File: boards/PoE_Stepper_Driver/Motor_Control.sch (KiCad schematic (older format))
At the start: 3 parts

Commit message: pretty much finished motor subsystem schematic
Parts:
- removed U?: TMC2660C-PA, QFP_2660C-PA_TRI, symbol TMC2660C-PA:TMC2660C-PA
- added C? (x2): 0.1uF, symbol device:C_Small
- added C? (x2): 10nF, symbol device:C_Small
- added C?: 470nF, symbol device:C_Small
- added C?: 220nF, symbol device:C_Small
- added C? (x2): 10uF, symbol device:C_Small
- added C? (x2): 100uF, symbol device:CP1_Small
- added R? (x3): 10k, symbol device:R_Small
- added R? (x2): 22, symbol device:R_Small
- added R? (x2): 75m, symbol device:R_Small
- added SW?: STO_L, symbol Switch:SW_SPST
- added SW?: STO_R, symbol Switch:SW_SPST
- added U?: TMC2660C-PA, QFP_2660C-PA_TRI, symbol TMC2660_2:TMC2660C-PA
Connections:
- net labels added: +12V, +3V3, CLK_2660, CLK_429, DIR, SPI1_CS, SPI1_MISO, SPI1_MOSI, SPI2_CS, SPI2_MISO, SPI2_MOSI, SPI2_SCK, STEP
- net labels removed: OA1, OA2, OB1, OB2
- wire segments 32 -> 150
- no-connect marks 0 -> 4
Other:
- moved on the sheet: J?, U?

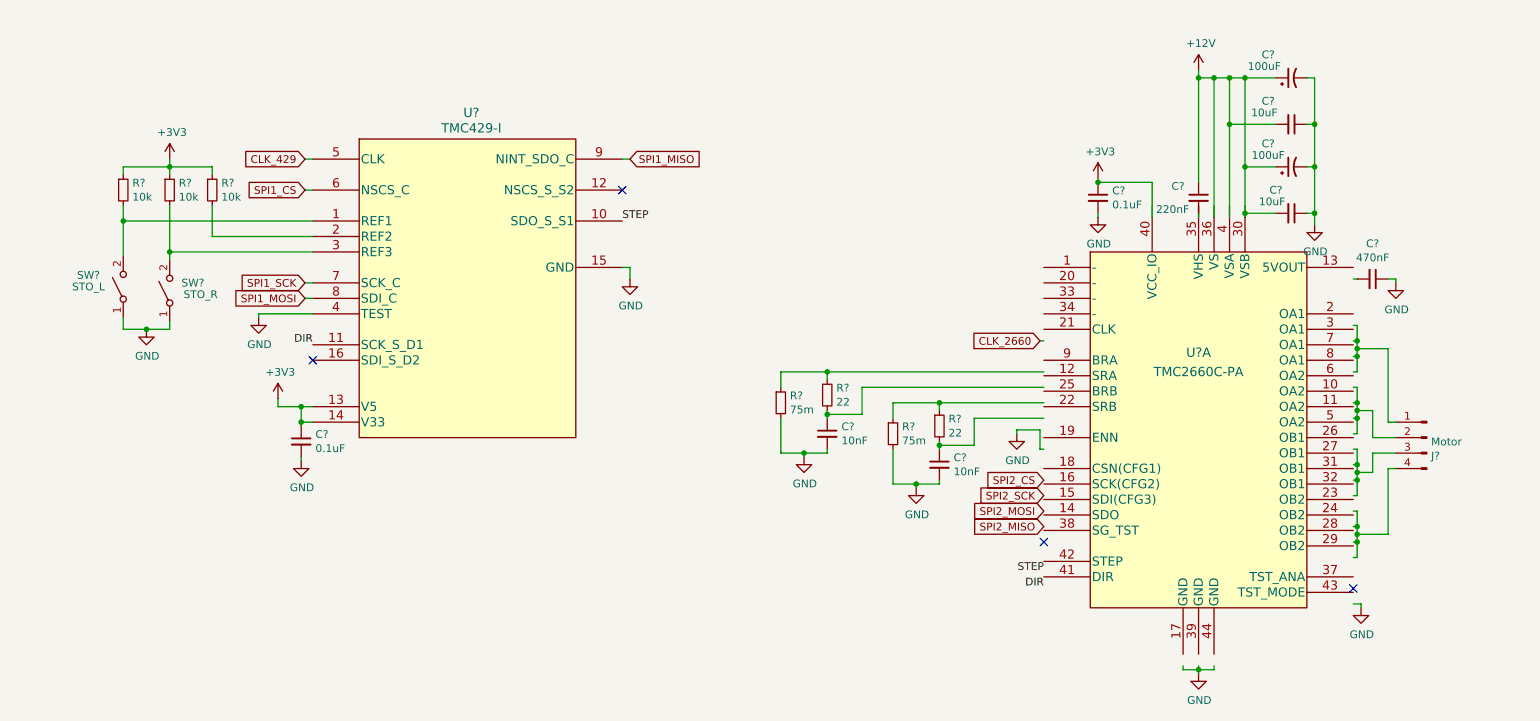
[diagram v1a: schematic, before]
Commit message: added actual phy
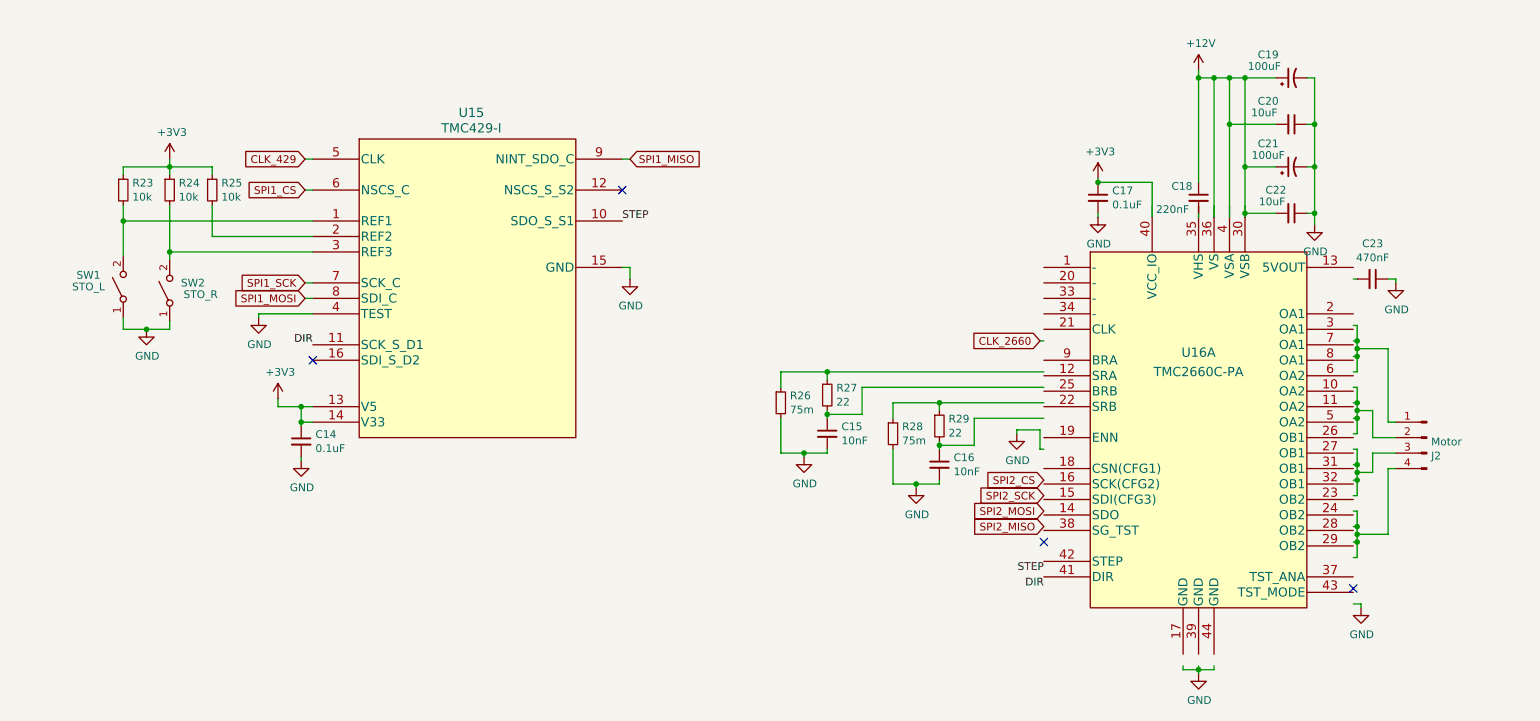
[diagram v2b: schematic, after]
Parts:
- gave numbers to parts that had none: 22
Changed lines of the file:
@@
 encoding utf-8
 Sheet 3 3
-Title ""
-Date ""
-Rev ""
+Title "PoE Stepper Driver"
+Date "2022-02-22"
+Rev "1.0"
 Comp ""
 Comment1 ""
@@
 $EndDescr
 $Comp
-L TMC429-I:TMC429-I U?
+L TMC429-I:TMC429-I U15
 U 1 1 6293383B
 P 2775 2300
-F 0 "U?" H 3800 2600 60  0000 C CNN
+F 0 "U15" H 3800 2600 60  0000 C CNN
 F 1 "TMC429-I" H 3800 2500 60  0000 C CNN
 F 2 "SSOP16_150MIL_TRI" H 3975 2540 60  0001 C CNN
@@
 SPI1_SCK
 $Comp
-L power:GND #PWR?
+L power:GND #PWR027
 U 1 1 62939459
 P 4825 3075
-F 0 "#PWR?" H 4825 2825 50  0001 C CNN
+F 0 "#PWR027" H 4825 2825 50  0001 C CNN
 F 1 "GND" H 4830 2902 50  0000 C CNN
 F 2 "" H 4825 3075 50  0001 C CNN
@@
 	4825 3000 4825 3075
 $Comp
-L power:GND #PWR?
+L power:GND #PWR034
 U 1 1 6293B082
 P 8500 5625
-F 0 "#PWR?" H 8500 5375 50  0001 C CNN
+F 0 "#PWR034" H 8500 5375 50  0001 C CNN
 F 1 "GND" H 8505 5452 50  0000 C CNN
 F 2 "" H 8500 5625 50  0001 C CNN
@@
 P 7850 2550
 AR Path="/6218906C" Ref="C?"  Part="1"
-AR Path="/6293177D/6218906C" Ref="C?"  Part="1"
-F 0 "C?" H 7942 2596 50  0000 L CNN
+AR Path="/6293177D/6218906C" Ref="C17"  Part="1"
+F 0 "C17" H 7942 2596 50  0000 L CNN
 F 1 "0.1uF" H 7942 2505 50  0000 L CNN
 F 2 "" H 7850 2550 50  0001 C CNN
@@
 P 7850 2425
 AR Path="/62189079" Ref="#PWR?"  Part="1"
-AR Path="/6293177D/62189079" Ref="#PWR?"  Part="1"
-F 0 "#PWR?" H 7850 2275 50  0001 C CNN
+AR Path="/6293177D/62189079" Ref="#PWR031"  Part="1"
+F 0 "#PWR031" H 7850 2275 50  0001 C CNN
 F 1 "+3V3" H 7865 2598 50  0000 C CNN
 F 2 "" H 7850 2425 50  0001 C CNN
@@
 P 2550 3850
 AR Path="/6218AB1A" Ref="#PWR?"  Part="1"
-AR Path="/6293177D/6218AB1A" Ref="#PWR?"  Part="1"
-F 0 "#PWR?" H 2550 3700 50  0001 C CNN
+AR Path="/6293177D/6218AB1A" Ref="#PWR025"  Part="1"
+F 0 "#PWR025" H 2550 3700 50  0001 C CNN
 F 1 "+3V3" H 2565 4023 50  0000 C CNN
 F 2 "" H 2550 3850 50  0001 C CNN
@@
 $EndComp
 $Comp
-L Switch:SW_SPST SW?
+L Switch:SW_SPST SW1
 U 1 1 6218BE4E
 P 1550 3125
-F 0 "SW?" V 1625 3350 50  0000 C CNN
+F 0 "SW1" V 1625 3350 50  0000 C CNN
 F 1 "STO_L" V 1550 3350 50  0000 C CNN
 F 2 "" H 1550 3125 50  0001 C CNN
@@
 $EndComp
 $Comp
-L Switch:SW_SPST SW?
+L Switch:SW_SPST SW2
 U 1 1 6218DF68
 P 1850 3150
-F 0 "SW?" V 1900 3000 50  0000 C CNN
+F 0 "SW2" V 1900 3000 50  0000 C CNN
 F 1 "STO_R" V 1825 2950 50  0000 C CNN
 F 2 "" H 1850 3150 50  0001 C CNN
@@
 $EndComp
 $Comp
-L power:GND #PWR?
+L power:GND #PWR024
 U 1 1 62192B2C
 P 2425 3325
-F 0 "#PWR?" H 2425 3075 50  0001 C CNN
+F 0 "#PWR024" H 2425 3075 50  0001 C CNN
 F 1 "GND" H 2430 3152 50  0000 C CNN
 F 2 "" H 2425 3325 50  0001 C CNN
@@
 NoConn ~ 4775 2500
 $Comp
-L device:C_Small C?
+L device:C_Small C14
 U 1 1 6219FF35
 P 2700 4125
-F 0 "C?" H 2608 4171 50  0000 R CNN
+F 0 "C14" H 2608 4171 50  0000 R CNN
 F 1 "0.1uF" H 2608 4080 50  0000 R CNN
 F 2 "" H 2700 4125 50  0001 C CNN
@@
 	2700 4000 2700 4025
 $Comp
-L power:GND #PWR?
+L power:GND #PWR026
 U 1 1 621A3739
 P 2700 4250
-F 0 "#PWR?" H 2700 4000 50  0001 C CNN
+F 0 "#PWR026" H 2700 4000 50  0001 C CNN
 F 1 "GND" H 2705 4077 50  0000 C CNN
 F 2 "" H 2700 4250 50  0001 C CNN
@@
 	2725 2300 2775 2300
 $Comp
-L power:GND #PWR?
+L power:GND #PWR022
 U 1 1 621E2D05
 P 1700 3400
-F 0 "#PWR?" H 1700 3150 50  0001 C CNN
+F 0 "#PWR022" H 1700 3150 50  0001 C CNN
 F 1 "GND" H 1705 3227 50  0000 C CNN
 F 2 "" H 1700 3400 50  0001 C CNN
@@
 	1550 2700 2775 2700
 $Comp
-L device:R_Small R?
+L device:R_Small R23
 U 1 1 621F05A6
 P 1550 2500
-F 0 "R?" H 1609 2546 50  0000 L CNN
+F 0 "R23" H 1609 2546 50  0000 L CNN
 F 1 "10k" H 1609 2455 50  0000 L CNN
 F 2 "" H 1550 2500 50  0001 C CNN
@@
 $EndComp
 $Comp
-L device:R_Small R?
+L device:R_Small R24
 U 1 1 621F9F83
 P 1850 2500
-F 0 "R?" H 1909 2546 50  0000 L CNN
+F 0 "R24" H 1909 2546 50  0000 L CNN
 F 1 "10k" H 1909 2455 50  0000 L CNN
 F 2 "" H 1850 2500 50  0001 C CNN
@@
 $EndComp
 $Comp
-L device:R_Small R?
+L device:R_Small R25
 U 1 1 62202E57
 P 2125 2500
-F 0 "R?" H 2184 2546 50  0000 L CNN
+F 0 "R25" H 2184 2546 50  0000 L CNN
 F 1 "10k" H 2184 2455 50  0000 L CNN
 F 2 "" H 2125 2500 50  0001 C CNN
@@
 P 1850 2300
 AR Path="/62208E6C" Ref="#PWR?"  Part="1"
-AR Path="/6293177D/62208E6C" Ref="#PWR?"  Part="1"
-F 0 "#PWR?" H 1850 2150 50  0001 C CNN
+AR Path="/6293177D/62208E6C" Ref="#PWR023"  Part="1"
+F 0 "#PWR023" H 1850 2150 50  0001 C CNN
 F 1 "+3V3" H 1865 2473 50  0000 C CNN
 F 2 "" H 1850 2300 50  0001 C CNN
@@
 P 9975 4100
 AR Path="/6292FF7A/62931FC4" Ref="J?"  Part="1"
-AR Path="/6293177D/62931FC4" Ref="J?"  Part="1"
-F 0 "J?" H 9947 3982 50  0000 R CNN
+AR Path="/6293177D/62931FC4" Ref="J2"  Part="1"
+F 0 "J2" H 9947 3982 50  0000 R CNN
 F 1 "Motor" H 9947 4073 50  0000 R CNN
 F 2 "" H 9975 4100 50  0001 C CNN
@@
 DIR
 $Comp
-L power:+12V #PWR?
+L power:+12V #PWR033
 U 1 1 622729F2
 P 8500 1725
-F 0 "#PWR?" H 8500 1575 50  0001 C CNN
+F 0 "#PWR033" H 8500 1575 50  0001 C CNN
 F 1 "+12V" H 8515 1898 50  0000 C CNN
 F 2 "" H 8500 1725 50  0001 C CNN
@@
 $EndComp
 $Comp
-L power:GND #PWR?
+L power:GND #PWR032
 U 1 1 6227F9C4
 P 7850 2675
-F 0 "#PWR?" H 7850 2425 50  0001 C CNN
+F 0 "#PWR032" H 7850 2425 50  0001 C CNN
 F 1 "GND" H 7855 2502 50  0000 C CNN
 F 2 "" H 7850 2675 50  0001 C CNN
@@
 	7850 2650 7850 2675
 $Comp
-L power:GND #PWR?
+L power:GND #PWR035
 U 1 1 62283BD0
 P 9250 2725
-F 0 "#PWR?" H 9250 2475 50  0001 C CNN
+F 0 "#PWR035" H 9250 2475 50  0001 C CNN
 F 1 "GND" H 9255 2552 50  0000 C CNN
 F 2 "" H 9250 2725 50  0001 C CNN
@@
 $EndComp
 $Comp
-L power:GND #PWR?
+L power:GND #PWR036
 U 1 1 622AA972
 P 9550 5200
-F 0 "#PWR?" H 9550 4950 50  0001 C CNN
+F 0 "#PWR036" H 9550 4950 50  0001 C CNN
 F 1 "GND" H 9555 5027 50  0000 C CNN
 F 2 "" H 9550 5200 50  0001 C CNN
@@
 SPI2_CS
 $Comp
-L device:R_Small R?
+L device:R_Small R27
 U 1 1 6238B615
 P 6100 3825
-F 0 "R?" H 6159 3871 50  0000 L CNN
+F 0 "R27" H 6159 3871 50  0000 L CNN
 F 1 "22" H 6159 3780 50  0000 L CNN
 F 2 "" H 6100 3825 50  0001 C CNN
@@
 $EndComp
 $Comp
-L device:C_Small C?
+L device:C_Small C15
 U 1 1 6238BD65
 P 6100 4075
-F 0 "C?" H 6192 4121 50  0000 L CNN
+F 0 "C15" H 6192 4121 50  0000 L CNN
 F 1 "10nF" H 6192 4030 50  0000 L CNN
 F 2 "" H 6100 4075 50  0001 C CNN
@@
 $EndComp
 $Comp
-L device:R_Small R?
+L device:R_Small R26
 U 1 1 623914C8
 P 5800 3875
-F 0 "R?" H 5859 3921 50  0000 L CNN
+F 0 "R26" H 5859 3921 50  0000 L CNN
 F 1 "75m" H 5859 3830 50  0000 L CNN
 F 2 "" H 5800 3875 50  0001 C CNN
@@
 $EndComp
 $Comp
-L power:GND #PWR?
+L power:GND #PWR028
 U 1 1 62397C91
 P 5950 4225
-F 0 "#PWR?" H 5950 3975 50  0001 C CNN
+F 0 "#PWR028" H 5950 3975 50  0001 C CNN
 F 1 "GND" H 5955 4052 50  0000 C CNN
 F 2 "" H 5950 4225 50  0001 C CNN
@@
 	6100 3950 6100 3975
 $Comp
-L device:R_Small R?
+L device:R_Small R29
 U 1 1 623F4B4C
 P 6825 4025
-F 0 "R?" H 6884 4071 50  0000 L CNN
+F 0 "R29" H 6884 4071 50  0000 L CNN
 F 1 "22" H 6884 3980 50  0000 L CNN
 F 2 "" H 6825 4025 50  0001 C CNN
@@
 $EndComp
 $Comp
-L device:C_Small C?
+L device:C_Small C16
 U 1 1 623F4B52
 P 6825 4275
-F 0 "C?" H 6917 4321 50  0000 L CNN
+F 0 "C16" H 6917 4321 50  0000 L CNN
 F 1 "10nF" H 6917 4230 50  0000 L CNN
 F 2 "" H 6825 4275 50  0001 C CNN
@@
 $EndComp
 $Comp
-L device:R_Small R?
+L device:R_Small R28
 U 1 1 623F4B58
 P 6525 4075
-F 0 "R?" H 6584 4121 50  0000 L CNN
+F 0 "R28" H 6584 4121 50  0000 L CNN
 F 1 "75m" H 6584 4030 50  0000 L CNN
 F 2 "" H 6525 4075 50  0001 C CNN
@@
 $EndComp
 $Comp
-L power:GND #PWR?
+L power:GND #PWR029
 U 1 1 623F4B5E
 P 6675 4425
-F 0 "#PWR?" H 6675 4175 50  0001 C CNN
+F 0 "#PWR029" H 6675 4175 50  0001 C CNN
 F 1 "GND" H 6680 4252 50  0000 C CNN
 F 2 "" H 6675 4425 50  0001 C CNN
@@
 NoConn ~ 9500 5075
 $Comp
-L power:GND #PWR?
+L power:GND #PWR037
 U 1 1 6246A24C
 P 9775 3100
-F 0 "#PWR?" H 9775 2850 50  0001 C CNN
+F 0 "#PWR037" H 9775 2850 50  0001 C CNN
 F 1 "GND" H 9780 2927 50  0000 C CNN
 F 2 "" H 9775 3100 50  0001 C CNN
@@
 	9500 3075 9525 3075
 $Comp
-L device:C_Small C?
+L device:C_Small C23
 U 1 1 62483CF6
 P 9625 3075
-F 0 "C?" V 9396 3075 50  0000 C CNN
+F 0 "C23" V 9396 3075 50  0000 C CNN
 F 1 "470nF" V 9487 3075 50  0000 C CNN
 F 2 "" H 9625 3075 50  0001 C CNN
@@
 	9775 3075 9775 3100
 $Comp
-L power:GND #PWR?
+L power:GND #PWR030
 U 1 1 624936CE
 P 7325 4075
-F 0 "#PWR?" H 7325 3825 50  0001 C CNN
+F 0 "#PWR030" H 7325 3825 50  0001 C CNN
 F 1 "GND" H 7330 3902 50  0000 C CNN
 F 2 "" H 7325 4075 50  0001 C CNN
@@
 NoConn ~ 7500 4775
 $Comp
-L device:C_Small C?
+L device:C_Small C18
 U 1 1 624C2AA3
 P 8500 2550
-F 0 "C?" H 8325 2625 50  0000 L CNN
+F 0 "C18" H 8325 2625 50  0000 L CNN
 F 1 "220nF" H 8225 2475 50  0000 L CNN
 F 2 "" H 8500 2550 50  0001 C CNN
@@
 	8500 2650 8500 2675
 $Comp
-L device:C_Small C?
+L device:C_Small C20
 U 1 1 624FC885
 P 9100 2075
-F 0 "C?" V 8950 1925 50  0000 C CNN
+F 0 "C20" V 8950 1925 50  0000 C CNN
 F 1 "10uF" V 9025 1900 50  0000 C CNN
 F 2 "" H 9100 2075 50  0001 C CNN
@@
 	8500 1725 8500 1775
 $Comp
-L device:C_Small C?
+L device:C_Small C22
 U 1 1 62501E5F
 P 9100 2650
-F 0 "C?" V 8950 2550 50  0000 C CNN
+F 0 "C22" V 8950 2550 50  0000 C CNN
 F 1 "10uF" V 9025 2525 50  0000 C CNN
 F 2 "" H 9100 2650 50  0001 C CNN
@@
 $EndComp
 $Comp
-L TMC2660_2:TMC2660C-PA U?
+L TMC2660_2:TMC2660C-PA U16
 U 1 1 6221AF33
 P 7500 3175
-F 0 "U?" H 8500 2800 60  0000 C CNN
+F 0 "U16" H 8500 2800 60  0000 C CNN
 F 1 "TMC2660C-PA" H 8500 2675 60  0000 C CNN
 F 2 "QFP_2660C-PA_TRI" H 8500 3515 60  0001 C CNN
@@
 $EndComp
 $Comp
-L device:CP1_Small C?
+L device:CP1_Small C21
 U 1 1 625835F8
 P 9100 2350
-F 0 "C?" V 9250 2500 50  0000 C CNN
+F 0 "C21" V 9250 2500 50  0000 C CNN
 F 1 "100uF" V 9175 2500 50  0000 C CNN
 F 2 "" H 9100 2350 50  0001 C CNN
@@
 $EndComp
 $Comp
-L device:CP1_Small C?
+L device:CP1_Small C19
 U 1 1 62584D8C
 P 9100 1775
-F 0 "C?" V 9250 1925 50  0000 C CNN
+F 0 "C19" V 9250 1925 50  0000 C CNN
 F 1 "100uF" V 9175 1950 50  0000 C CNN
 F 2 "" H 9100 1775 50  0001 C CNN

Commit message: added dp83848 phy and more caps
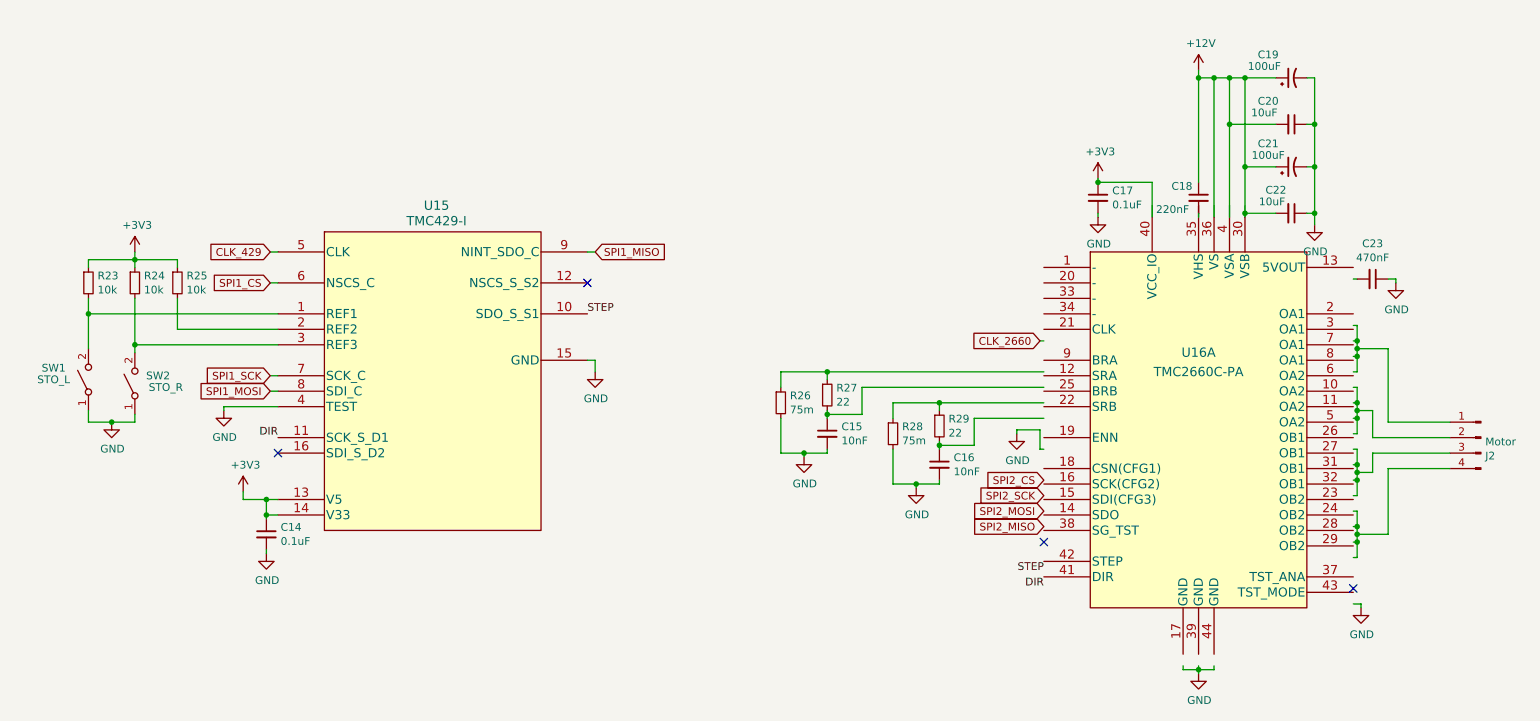
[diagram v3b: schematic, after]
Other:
- moved on the sheet: C14, J2, R23, R24, R25, SW1, SW2, U15

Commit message: started board layout
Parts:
- removed SW1: STO_L, symbol Switch:SW_SPST
- removed SW2: STO_R, symbol Switch:SW_SPST
- added J3: Limits, symbol Connector:Conn_01x04_Male
- C14, C17: footprint (none) -> Capacitor_SMD:C_0805_2012Metric_Pad1.15x1.40mm_HandSolder
- J2: footprint (none) -> Connector_JST:JST_PH_B4B-PH-K_1x04_P2.00mm_Vertical
- U15: footprint SSOP16_150MIL_TRI -> Package_SO:SSOP-16_3.9x4.9mm_P0.635mm
- U16: footprint QFP_2660C-PA_TRI -> Package_QFP:PQFP-44_10x10mm_P0.8mm
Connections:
- wire segments 150 -> 153
- no-connect marks 4 -> 8
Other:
- moved on the sheet: C14, C15, C16, C17, C18, C19, C20, C21, C22, C23, J2, R23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
